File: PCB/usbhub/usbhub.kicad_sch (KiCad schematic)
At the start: 35 parts, among them U1 SL2.1S, U2 SL2.1S

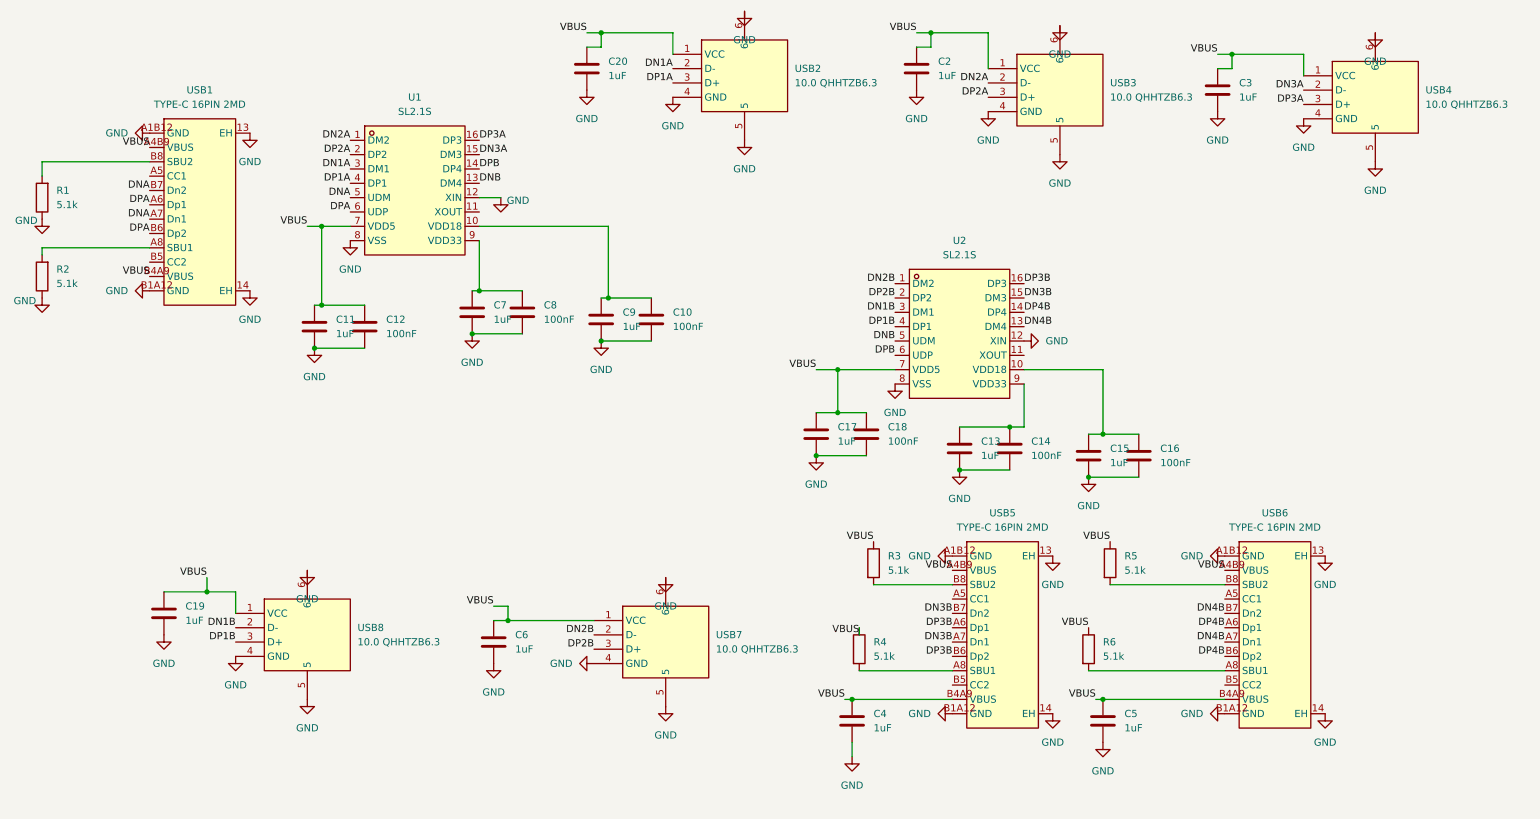
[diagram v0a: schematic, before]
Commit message: unmixup cc1 with sbu1
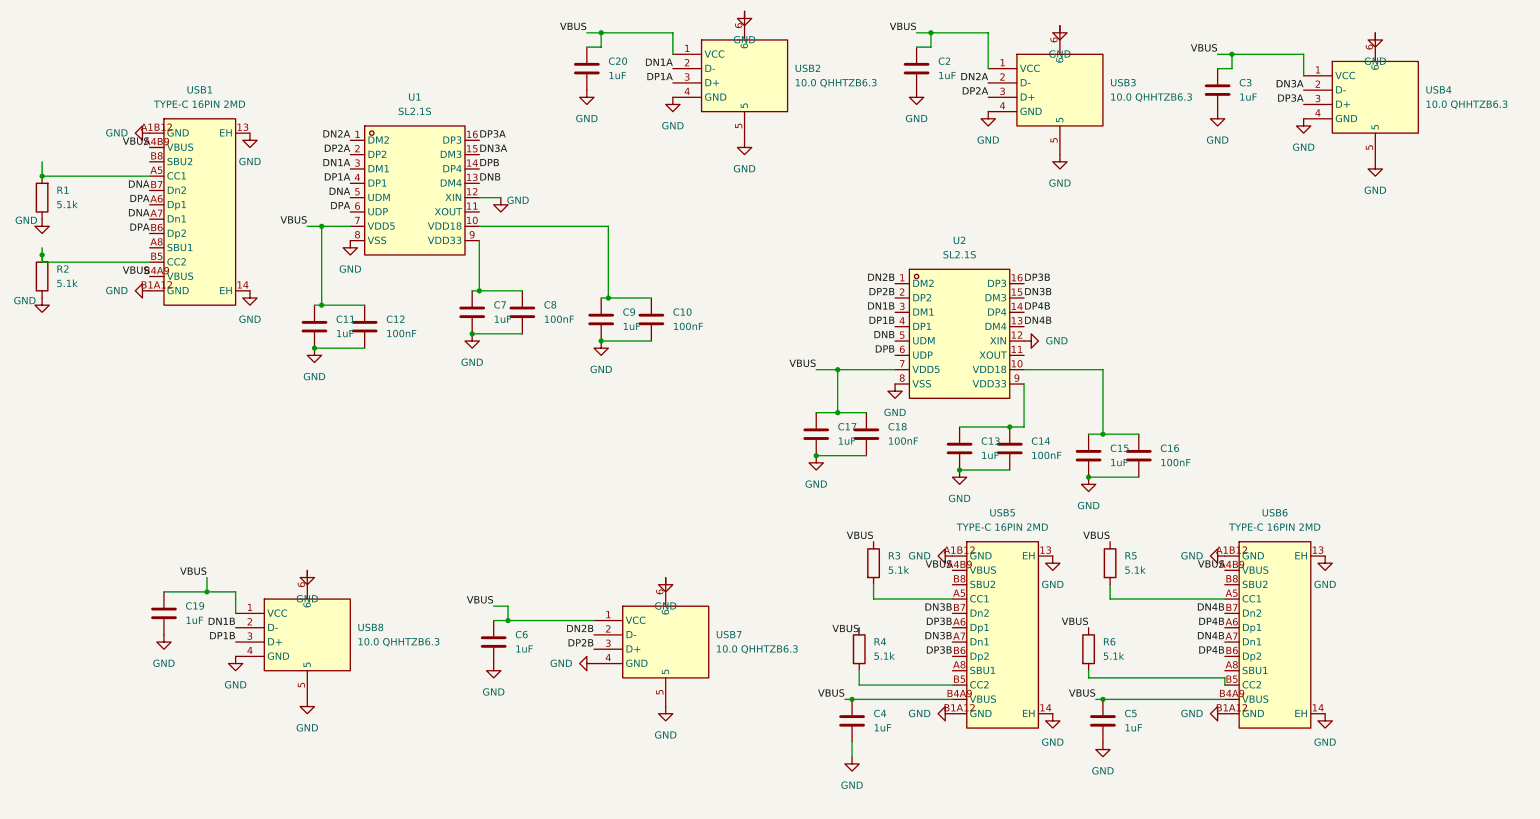
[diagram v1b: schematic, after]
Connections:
- net at USB1.A5 (CC1): now also R1.2
- net at USB1.A8 (SBU1): no longer R2.2
- net at USB1.B5 (CC2): now also R2.2
- net at USB1.B8 (SBU2): no longer R1.2
- net at USB5.A5 (CC1): now also R3.2
- net at USB5.A8 (SBU1): no longer R4.2
- net at USB5.B5 (CC2): now also R4.2
- net at USB5.B8 (SBU2): no longer R3.2
- net at USB6.A5 (CC1): now also R5.2
- net at USB6.A8 (SBU1): no longer R6.2
- net at USB6.B5 (CC2): now also R6.2
- net at USB6.B8 (SBU2): no longer R5.2
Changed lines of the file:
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@@
+	)
+	(junction
+		(at 21.59 55.88)
+		(diameter 0)
+		(color 0 0 0 0)
+	)
+	(junction
+		(at 21.59 41.91)
+		(diameter 0)
+		(color 0 0 0 0)
 	)
 	(junction
@@
 	(wire
 		(pts
+			(xy 40.64 57.15) (xy 21.59 57.15)
+		)
+		(stroke
+			(width 0)
+			(type default)
+		)
+	)
+	(wire
+		(pts
 			(xy 121.92 50.8) (xy 99.06 50.8)
 		)
@@
 	(wire
 		(pts
+			(xy 21.59 41.91) (xy 40.64 41.91)
+		)
+		(stroke
+			(width 0)
+			(type default)
+		)
+	)
+	(wire
+		(pts
 			(xy 232.41 20.32) (xy 245.11 20.32)
 		)
@@
 	(wire
 		(pts
-			(xy 182.88 129.54) (xy 166.37 129.54)
+			(xy 207.01 130.81) (xy 231.14 130.81)
 		)
 		(stroke
@@
 	(wire
 		(pts
+			(xy 210.82 114.3) (xy 210.82 116.84)
+		)
+		(stroke
+			(width 0)
+			(type default)
+		)
+	)
+	(wire
+		(pts
 			(xy 176.53 16.51) (xy 179.07 16.51)
 		)
@@
 	(wire
 		(pts
+			(xy 231.14 130.81) (xy 231.14 132.08)
+		)
+		(stroke
+			(width 0)
+			(type default)
+		)
+	)
+	(wire
+		(pts
 			(xy 184.15 86.36) (xy 193.04 86.36)
 		)
@@
 	(wire
 		(pts
+			(xy 210.82 116.84) (xy 231.14 116.84)
+		)
+		(stroke
+			(width 0)
+			(type default)
+		)
+	)
+	(wire
+		(pts
+			(xy 21.59 55.88) (xy 21.59 57.15)
+		)
+		(stroke
+			(width 0)
+			(type default)
+		)
+	)
+	(wire
+		(pts
 			(xy 104.14 120.65) (xy 119.38 120.65)
 		)
@@
 	(wire
 		(pts
-			(xy 40.64 39.37) (xy 21.59 39.37)
+			(xy 182.88 116.84) (xy 168.91 116.84)
 		)
 		(stroke
@@
 	(wire
 		(pts
-			(xy 231.14 114.3) (xy 210.82 114.3)
-		)
-		(stroke
-			(width 0)
-			(type default)
-		)
-	)
-	(wire
-		(pts
-			(xy 40.64 54.61) (xy 21.59 54.61)
-		)
-		(stroke
-			(width 0)
-			(type default)
-		)
-	)
-	(wire
-		(pts
-			(xy 182.88 114.3) (xy 168.91 114.3)
-		)
-		(stroke
-			(width 0)
-			(type default)
-		)
-	)
-	(wire
-		(pts
 			(xy 163.83 134.62) (xy 165.1 134.62)
 		)
@@
 	(wire
 		(pts
+			(xy 166.37 129.54) (xy 166.37 132.08)
+		)
+		(stroke
+			(width 0)
+			(type default)
+		)
+	)
+	(wire
+		(pts
 			(xy 50.8 115.57) (xy 55.88 115.57)
 		)
@@
 	(wire
 		(pts
-			(xy 231.14 129.54) (xy 207.01 129.54)
+			(xy 207.01 129.54) (xy 207.01 130.81)
 		)
 		(stroke
@@
 	(wire
 		(pts
+			(xy 166.37 132.08) (xy 182.88 132.08)
+		)
+		(stroke
+			(width 0)
+			(type default)
+		)
+	)
+	(wire
+		(pts
 			(xy 158.75 76.2) (xy 162.56 76.2)
 		)
@@
 		)
 		(stroke
+			(width 0)
+			(type default)
+		)
+	)
+	(wire
+		(pts
+			(xy 168.91 116.84) (xy 168.91 114.3)
+		)
+		(stroke

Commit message: minus/plus rename
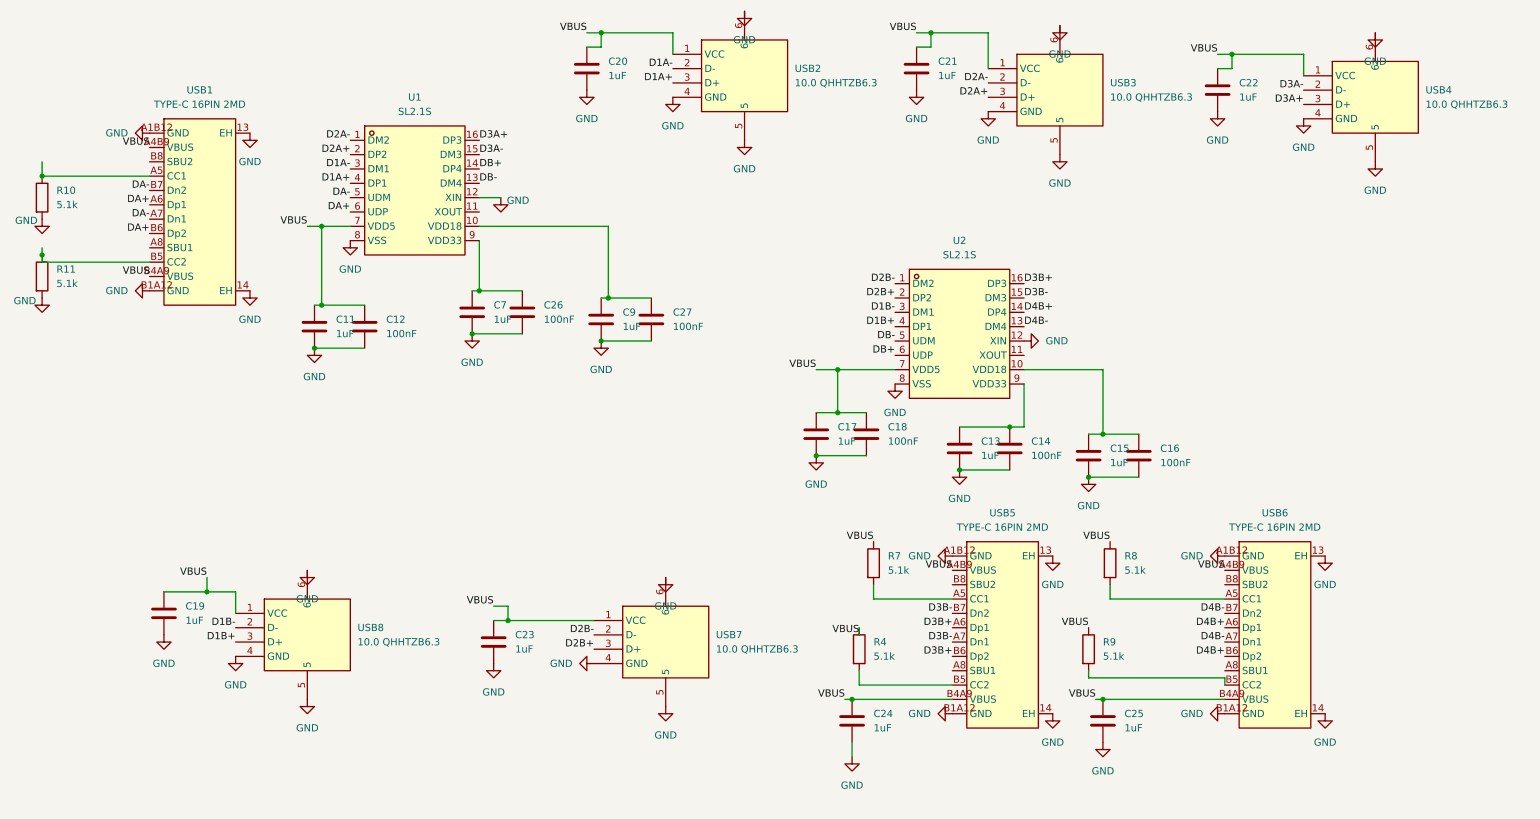
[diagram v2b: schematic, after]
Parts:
- removed C10, C8: 100nF, symbol Device:C
- removed C2, C3, C4, C5, C6: 1uF, symbol Device:C
- removed R1, R2, R3, R5, R6: 5.1k, symbol Device:R
- added C21, C22, C23, C24, C25: 1uF, lcsc:C0402, symbol Device:C
- added C26, C27: 100nF, lcsc:C0402, symbol Device:C
- added R10, R11, R7, R8, R9: 5.1k, lcsc:R0402, symbol Device:R
- C11, C13, C15, C17, C19, C20, C7, C9: footprint (none) -> lcsc:C0402; LCSC Part (none) -> C29266
- C12, C14, C16, C18: footprint (none) -> lcsc:C0402; LCSC Part (none) -> C60474
- R4: footprint (none) -> lcsc:R0402; LCSC Part (none) -> C105872
- U1, U2: footprint easyeda2kicad:SSOP-16_L4.6-W2.6-P0.53-LS4.0-BL -> lcsc:SSOP-16_L4.6-W2.6-P0.53-LS4.0-BL
- USB1, USB5, USB6: footprint easyeda2kicad:USB-C-SMD_TYPE-C-16PIN-2MD-073 -> lcsc:USB-C-SMD_TYPE-C-16PIN-2MD-073
- USB2, USB3, USB4, USB7, USB8: footprint easyeda2kicad:USB-A-TH_10.0QHHTZB6.3 -> lcsc:USB-A-TH_10.0QHHTZB6.3
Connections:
- net GND: now also C21.2, C22.2, C23.2, C24.2, C25.2, C26.2, C27.2, R10.2, R11.2
- net VBUS: now also C21.1, C22.1, C23.1, C24.1, C25.1, R7.1, R8.1, R9.1
- net at USB1.A5 (CC1): now also R10.1
- net at USB1.B5 (CC2): now also R11.1
- net at C9.1, U1.10 (VDD18): now also C27.1
- net at C7.1, U1.9 (VDD33): now also C26.1
- net at USB5.A5 (CC1): now also R7.2
- net at USB6.A5 (CC1): now also R8.2
- net at USB6.B5 (CC2): now also R9.2
- net DN1A renamed D1A-
- net DN1B renamed D1B-
- net DN2A renamed D2A-
- net DN2B renamed D2B-
- net DN3A renamed D3A-
- net DN3B renamed D3B-
- net DN4B renamed D4B-
- net DNA renamed DA-
- net DNB renamed DB-
- net DP1A renamed D1A+
- net DP1B renamed D1B+
- net DP2A renamed D2A+
- net DP2B renamed D2B+
- net DP3A renamed D3A+
- net DP3B renamed D3B+
- net DP4B renamed D4B+
- net DPA renamed DA+
- net DPB renamed DB+

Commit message: placement
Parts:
- renumbered USB1 to usb1_upstream1
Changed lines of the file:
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@@
 		(dnp no)
 		(fields_autoplaced yes)
-		(property "Reference" "USB1"
+		(property "Reference" "usb1_upstream1"
 			(at 49.53 26.67 0)
 			(show_name no)
@@
 			(project "usbhub"
 				(path "/32d624bb-c978-4570-8c92-7fbd28df6f08"
-					(reference "USB1")
+					(reference "usb1_upstream1")
 					(unit 1)
 				)

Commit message: update all the steps
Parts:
- added H1, H2: MountingHole, MountingHole:MountingHole_3.2mm_M3, symbol Mechanical:MountingHole
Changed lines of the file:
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@@
+	)
+	(symbol
+		(lib_id "Mechanical:MountingHole")
+		(at 60.96 151.13 0)
+		(unit 1)
+		(body_style 1)
+		(exclude_from_sim no)
+		(in_bom no)
+		(on_board yes)
+		(in_pos_files yes)
+		(dnp no)
+		(fields_autoplaced yes)
+		(property "Reference" "H2"
+			(at 63.5 149.8599 0)
+			(show_name no)
+			(do_not_autoplace no)
+			(effects
+				(font
+					(size 1.27 1.27)
+				)
+				(justify left)
+			)
+		)
+		(property "Value" "MountingHole"
+			(at 63.5 152.3999 0)
+			(show_name no)
+			(do_not_autoplace no)
+			(effects
+				(font
+					(size 1.27 1.27)
+				)
+				(justify left)
+			)
+		)
+		(property "Footprint" "MountingHole:MountingHole_3.2mm_M3"
+			(at 60.96 151.13 0)
+			(hide yes)
+			(show_name no)
+			(do_not_autoplace no)
+			(effects
+				(font
+					(size 1.27 1.27)
+				)
+			)
+		)
+		(property "Datasheet" ""
+			(at 60.96 151.13 0)
+			(hide yes)
+			(show_name no)
+			(do_not_autoplace no)
+			(effects
+				(font
+					(size 1.27 1.27)
+				)
+			)
+		)
+		(property "Description" "Mounting Hole without connection"
+			(at 60.96 151.13 0)
+			(hide yes)
+			(show_name no)
+			(do_not_autoplace no)
+			(effects
+				(font
+					(size 1.27 1.27)
+				)
+			)
+		)
+		(instances
+			(project "usbhub"
+				(path "/32d624bb-c978-4570-8c92-7fbd28df6f08"
+					(reference "H2")
+					(unit 1)
+				)
+			)
+		)
 	)
 	(symbol
@@
 					(unit 1)
 				)
+			)
+		)
+	)
+	(symbol
+		(lib_id "Mechanical:MountingHole")
+		(at 45.72 151.13 0)
+		(unit 1)
+		(body_style 1)
+		(exclude_from_sim no)
+		(in_bom no)
+		(on_board yes)
+		(in_pos_files yes)
+		(dnp no)
+		(fields_autoplaced yes)
+		(property "Reference" "H1"
+			(at 48.26 149.8599 0)
+			(show_name no)
+			(do_not_autoplace no)
+			(effects
+				(font
+					(size 1.27 1.27)
+				)
+				(justify left)
+			)
+		)
+		(property "Value" "MountingHole"
+			(at 48.26 152.3999 0)
+			(show_name no)
+			(do_not_autoplace no)
+			(effects
+				(font
+					(size 1.27 1.27)
+				)
+				(justify left)
+			)
+		)
+		(property "Footprint" "MountingHole:MountingHole_3.2mm_M3"
+			(at 45.72 151.13 0)
+			(hide yes)
+			(show_name no)
+			(do_not_autoplace no)
+			(effects
+				(font
+					(size 1.27 1.27)
+				)
+			)
+		)
+		(property "Datasheet" ""
+			(at 45.72 151.13 0)
+			(hide yes)
+			(show_name no)
+			(do_not_autoplace no)
+			(effects
+				(font
+					(size 1.27 1.27)
+				)
+			)
+		)
+		(property "Description" "Mounting Hole without connection"
+			(at 45.72 151.13 0)
+			(hide yes)
+			(show_name no)
+			(do_not_autoplace no)
+			(effects
+				(font
+					(size 1.27 1.27)
+				)
+			)
+		)
+		(instances
+			(project "usbhub"
+				(path "/32d624bb-c978-4570-8c92-7fbd28df6f08"
+					(reference "H1")
+					(unit 1)
+				)
